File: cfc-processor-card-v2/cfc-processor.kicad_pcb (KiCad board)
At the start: 4 copper layers, 99.8 x 94.6 mm, 196 parts, among them J1 TFM-120-01-L-D-RA, J2 2-1734592-0, J3 J-SAMTEC-TFM-110-X1-XXX-D-RA, J4 GRPB041VWVN-RC, J5 DM3BT-DSF-PEJS, J6 Conn_01x02, Q1 DMP2240UDM, Q2 DMN2050LQ-7, Q3 DMPH2040UVTQ-7, Q4 DMPH2040UVTQ-7, Q5 DMN2050LQ-7, Q6 MMBT2907, U1 MAX7310ATE+, U10 RCLAMP0504FB, U11 TCAN330, U12 SFEM016GB1EA1TO-I-GE-121-STD, U13 DS90CR218AMTD/NOPB, U2 MIC842LYC5, U3 MIC842LYC5, U4 TS5A21366, U5 MAX4211FETE, U6 TPS62112, U7 OSD3358-1G-ISM, U8 SN74AUC1G07DCKR, U9 TLVH431, Y1 ECS-240-12-30BQ-AEN-TR, Y2 ABS07-32.768KHZ-T

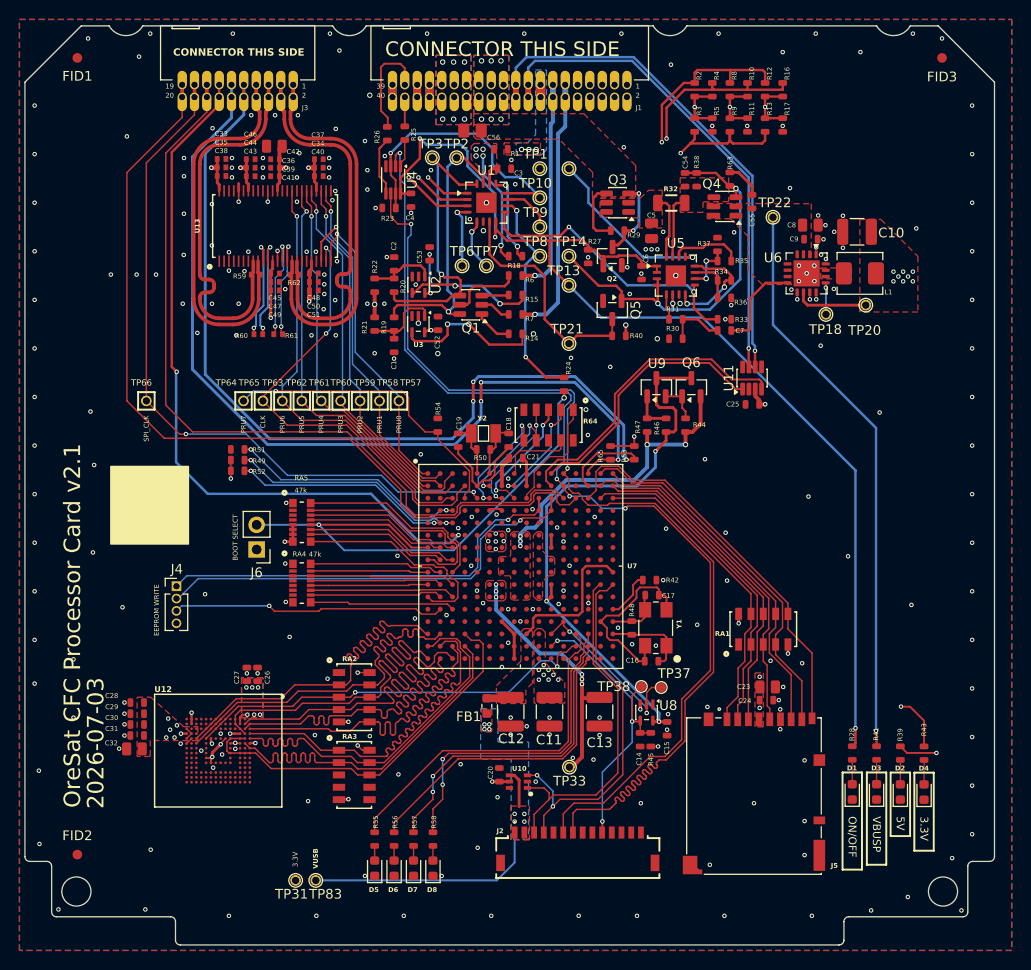
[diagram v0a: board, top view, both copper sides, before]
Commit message: Update
Updated BOM, couple of fixes on OPD. Minor routing and layout changes. Removed logic gates from sensor card.
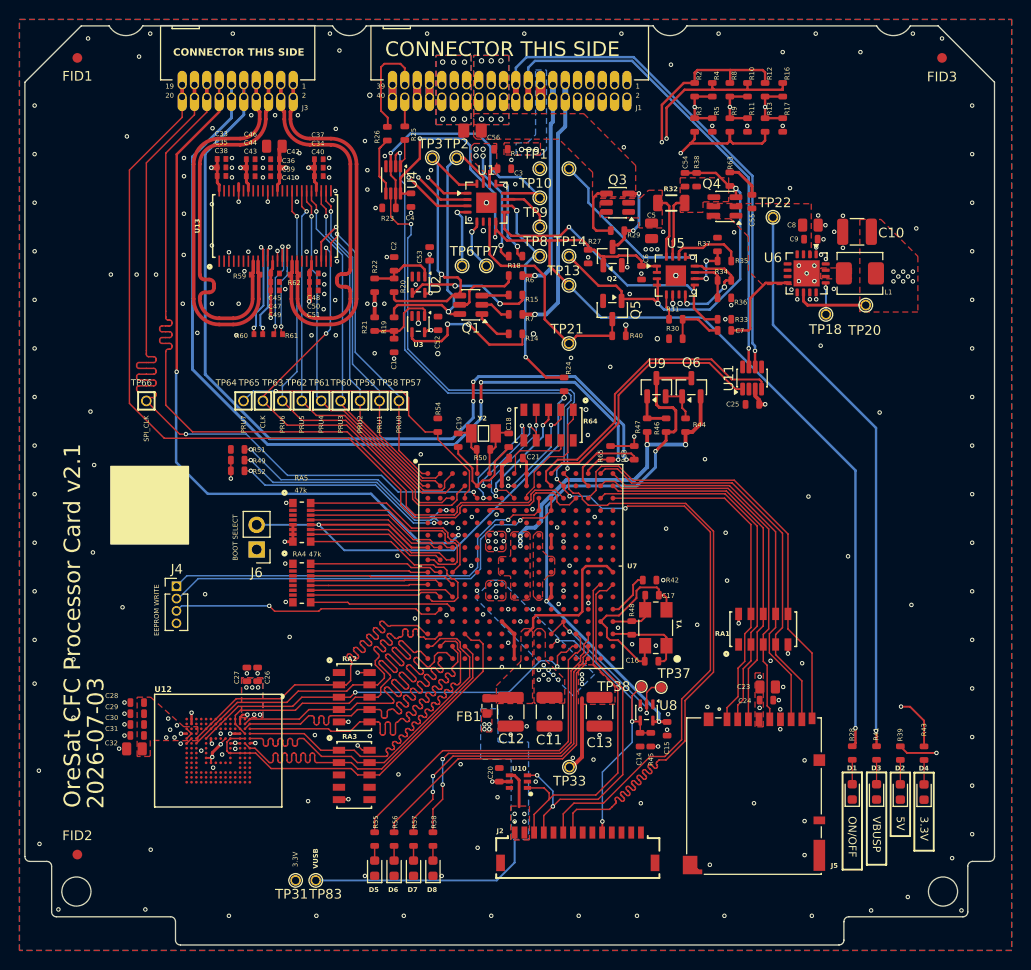
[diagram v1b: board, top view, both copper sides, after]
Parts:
- Q1: value DMP2240UDM -> DMP2110UVTQ-7
- R10, R11, R12, R13, R16, R17, R2, R3, R4, R5, R8, R9: value 1k -> 100
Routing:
- net VDD: track 27.2 -> 7.80 mm
- net /SPI1_CLK: track 73.0 -> 85.2 mm
- net /SPI1_MISO: track 83.4 -> 88.3 mm
- net Net-(J5-DAT2): track 32.2 -> 36.4 mm
- net Net-(J5-DAT3/CS): track 34.2 -> 38.4 mm
- net Net-(J5-DAT1): track 38.0 -> 42.2 mm
- net Net-(J5-CLK): track 35.4 -> 39.6 mm
- net Net-(J5-CD#): track 41.8 -> 46.0 mm
- net Net-(J5-DAT0/DO): track 35.6 -> 39.7 mm
- net Net-(J5-CMD/DI): track 33.4 -> 37.6 mm
- net /OSD3358: SIP C/UART-TX: track 107.1 -> 108.9 mm
- net /OSD3358: SIP C/UART-RX: track 110.6 -> 112.4 mm
- net /Power (OPD)/ON/~{OFF}: track 116.8 -> 117.3 mm
- added copper zone on B.Cu, net VDD

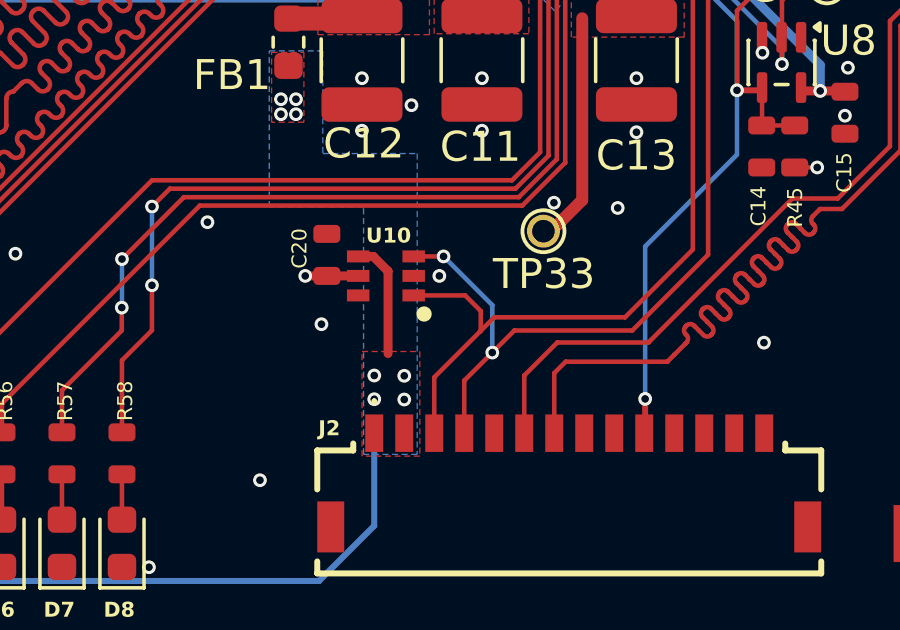
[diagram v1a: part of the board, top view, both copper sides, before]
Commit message: Small update
Fixed minor issue with voltage clamp on usb line. Added nreset clamp and changed VBUS pin to USB voltage bus
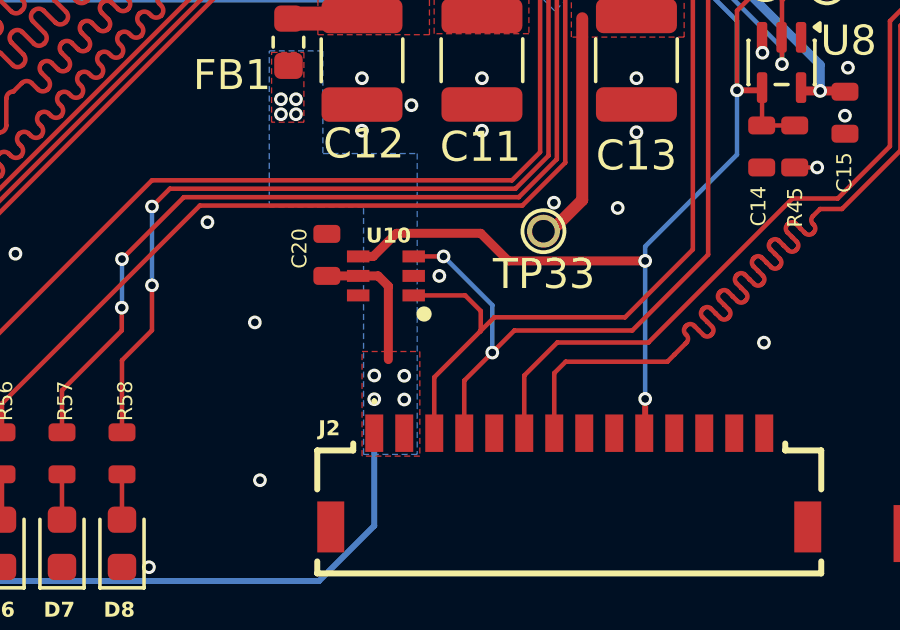
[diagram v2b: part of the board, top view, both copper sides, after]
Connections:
- C20 pad 1: 3.3V -> /OSD3358: SIP B/USB_CLI_VBUS
- U10 pad 4: /OSD3358: SIP B/USB_CLI_VBUS -> /OSD3358: SIP A (PWR)/NRESET
- U10 pad 5: 3.3V -> /OSD3358: SIP B/USB_CLI_VBUS
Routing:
- net /OSD3358: SIP A (PWR)/NRESET: track 33.3 -> 43.6 mm, vias 3 -> 4
- net 3.3V: track 62.6 -> 60.8 mm, vias 35 -> 34
- net /OSD3358: SIP B/USB_CLI_VBUS: track 27.7 -> 28.4 mm
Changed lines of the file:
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@@
 			(size 0.4 0.75)
 			(layers "F.Cu" "F.Mask")
-			(net "/OSD3358: SIP B/USB_CLI_VBUS")
+			(net "/OSD3358: SIP A (PWR)/NRESET")
 			(pinfunction "I3_4")
 			(pintype "bidirectional")
@@
 			(size 0.4 0.75)
 			(layers "F.Cu" "F.Mask")
-			(net "3.3V")
+			(net "/OSD3358: SIP B/USB_CLI_VBUS")
 			(pinfunction "VCC_5")
 			(pintype "power_in")
@@
 			(layers "F.Cu" "F.Mask" "F.Paste")
 			(roundrect_rratio 0.25)
-			(net "3.3V")
+			(net "/OSD3358: SIP B/USB_CLI_VBUS")
 			(pintype "passive")
 			(thermal_bridge_angle 0)
@@
 	)
 	(via
-		(at 147.25 137.1)
+		(at 145.03 137.04)
 		(size 0.4572)
 		(drill 0.254)
@@
 	)
 	(segment
-		(start 148.475 135.49)
-		(end 147.43 135.49)
-		(width 0.3)
-		(layer "F.Cu")
-		(net "3.3V")
-	)
-	(segment
 		(start 117.2511 133.0536)
 		(end 117.7886 133.0536)
@@
 	)
 	(segment
-		(start 147.43 135.49)
-		(end 146.71 135.49)
-		(width 0.3)
-		(layer "F.Cu")
-		(net "3.3V")
-	)
-	(segment
 		(start 161.32 100.95)
 		(end 161.32 99.97)
@@
 	)
 	(via
-		(at 146.71 135.49)
-		(size 0.4572)
-		(drill 0.254)
-		(layers "F.Cu" "B.Cu")
-		(net "3.3V")
-	)
-	(via
 		(at 130.6336 78.4061)
 		(size 0.4572)
@@
 	)
 	(segment
+		(start 153.48 134.99)
+		(end 158.04 134.99)
+		(width 0.3)
+		(layer "F.Cu")
+		(net "/OSD3358: SIP A (PWR)/NRESET")
+	)
+	(segment
+		(start 149.747 134.07)
+		(end 152.56 134.07)
+		(width 0.3)
+		(layer "F.Cu")
+		(net "/OSD3358: SIP A (PWR)/NRESET")
+	)
+	(segment
+		(start 152.56 134.07)
+		(end 153.48 134.99)
+		(width 0.3)
+		(layer "F.Cu")
+		(net "/OSD3358: SIP A (PWR)/NRESET")
+	)
+	(segment
 		(start 161.925 130.475)
 		(end 163.025 130.475)
@@
 	)
 	(segment
+		(start 148.475 134.84)
+		(end 148.977 134.84)
+		(width 0.3)
+		(layer "F.Cu")
+		(net "/OSD3358: SIP A (PWR)/NRESET")
+	)
+	(segment
 		(start 161.1011 129.3036)
 		(end 161.8511 129.3036)
@@
 	)
 	(segment
+		(start 148.977 134.84)
+		(end 149.747 134.07)
+		(width 0.3)
+		(layer "F.Cu")
+		(net "/OSD3358: SIP A (PWR)/NRESET")
+	)
+	(segment
 		(start 161.9375 129.325)
 		(end 161.9375 130.4625)
@@
 	)
 	(via
+		(at 158.04 134.99)
+		(size 0.4572)
+		(drill 0.254)
+		(layers "F.Cu" "B.Cu")
+		(net "/OSD3358: SIP A (PWR)/NRESET")
+	)
+	(via
 		(at 161.1011 129.3036)
 		(size 0.4572)
@@
 	)
 	(segment
-		(start 158.04 139.59)
+		(start 158.04 134.99)
 		(end 158.04 134.51)
 		(width 0.1524)
@@
 	)
 	(segment
+		(start 158.04 139.59)
+		(end 158.04 134.99)
+		(width 0.1524)
+		(layer "B.Cu")
+		(net "/OSD3358: SIP A (PWR)/NRESET")
+	)
+	(segment
 		(start 153.4136 120.9911)
 		(end 155.1011 120.9911)
@@
 	)
 	(segment
-		(start 148.977 134.84)
-		(end 149.47 135.333)
+		(start 148.475 135.49)
+		(end 147.43 135.49)
 		(width 0.3)
 		(layer "F.Cu")
@@
 	)
 	(segment
-		(start 149.47 135.333)
-		(end 149.47 138.08)
+		(start 149.14 135.49)
+		(end 149.48 135.83)
 		(width 0.3)
 		(layer "F.Cu")
@@
 	)
 	(segment
-		(start 148.475 134.84)
-		(end 148.977 134.84)
+		(start 148.475 135.49)
+		(end 149.14 135.49)
+		(width 0.3)
+		(layer "F.Cu")
+		(net "/OSD3358: SIP B/USB_CLI_VBUS")
+	)
+	(segment
+		(start 149.48 135.83)
+		(end 149.48 138.28)
 		(width 0.3)
 		(layer "F.Cu")
